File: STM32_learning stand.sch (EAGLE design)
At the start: 131 parts, among them J1 Power in, J10 RS-485_1, J11 RS-485_2, J12 FD CAN 1, J13 FD CAN 2, J15 Motor, J2 ST-link, J3 Encoder, J4 BMS_interface, J5 S6B-PH-K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

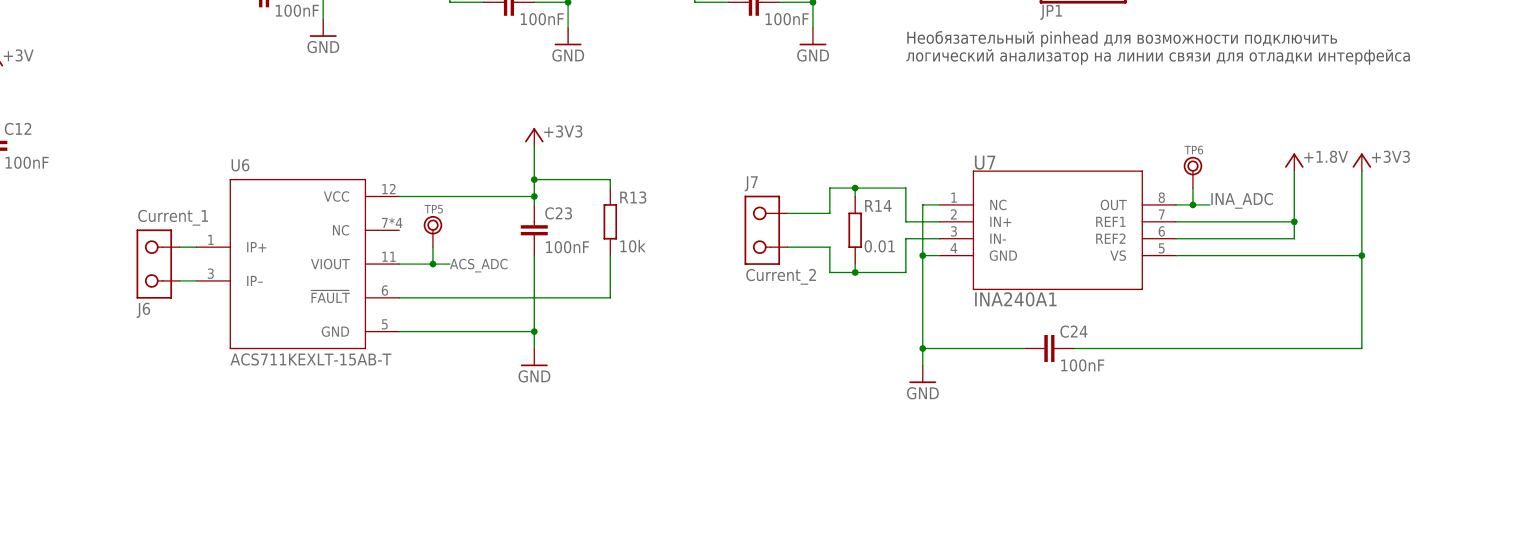
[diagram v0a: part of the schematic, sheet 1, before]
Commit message: Added calibration and better current measurement organiztion
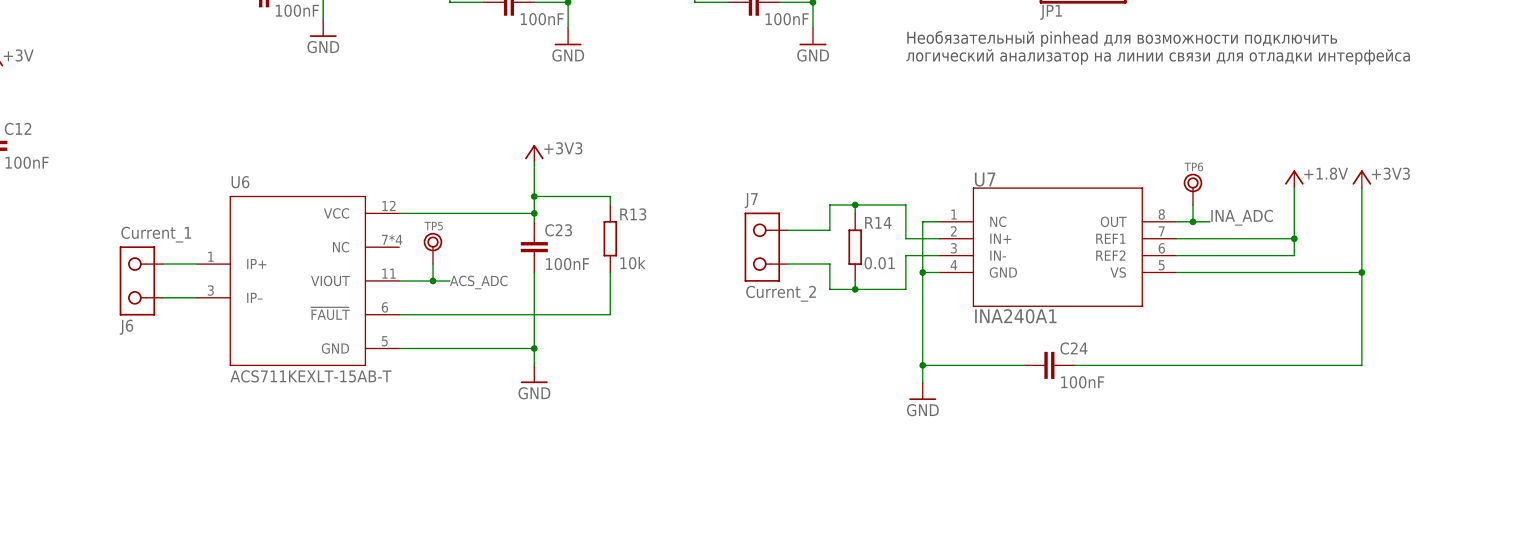
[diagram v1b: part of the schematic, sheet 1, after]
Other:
- moved on the sheet: C23, C24, J6, J7, R13, R14, TP5, TP6, U6, U7
